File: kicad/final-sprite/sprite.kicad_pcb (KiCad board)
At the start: 4 copper layers, 35 x 44.6 mm, 64 parts, among them J1 M20-7910442R, U1 CC430F513X, U2 LSM9DS1, U3 SPRITETCXO_TCXO_7Z, U4 DRV8837, U5 ADP5092, U6 DRV8837, U7 DRV8837, X1 SPRITEPIN_SPRITE_PIN, X2 SPRITEPIN_SPRITE_PIN

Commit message: Fix inductor
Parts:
- moved TP1 7.53 mm to (136.0, 114.0)
- moved L1 1.99 mm to (126.4, 91.4)
- moved D4 0.63 mm to (143.1, 101.6)
- moved L4 0.17 mm to (141.2, 84.6)
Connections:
- net Net-(L1-PadP$2) renamed /SWN
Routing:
- net Net-(R22-Pad1): track 305.9 -> 310.8 mm, vias 3 -> 4
- net GND: track 14.8 -> 16.0 mm, vias 39 -> 40
- net Net-(L3-Pad1): track 18.5 -> 19.5 mm
- net Net-(L4-Pad2): track 21.6 -> 20.6 mm
- net VCC: track 130.2 -> 129.5 mm
- net /REGGOOD: track 16.8 -> 17.4 mm
- net VCCINT: track 93.9 -> 93.2 mm
- net /RST: track 37.9 -> 38.5 mm
- net (no net): vias 0 -> 1
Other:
- net class Power added: clearance 0.1524, trace_width 0.3048, via_dia 0.5588, via_drill 0.254

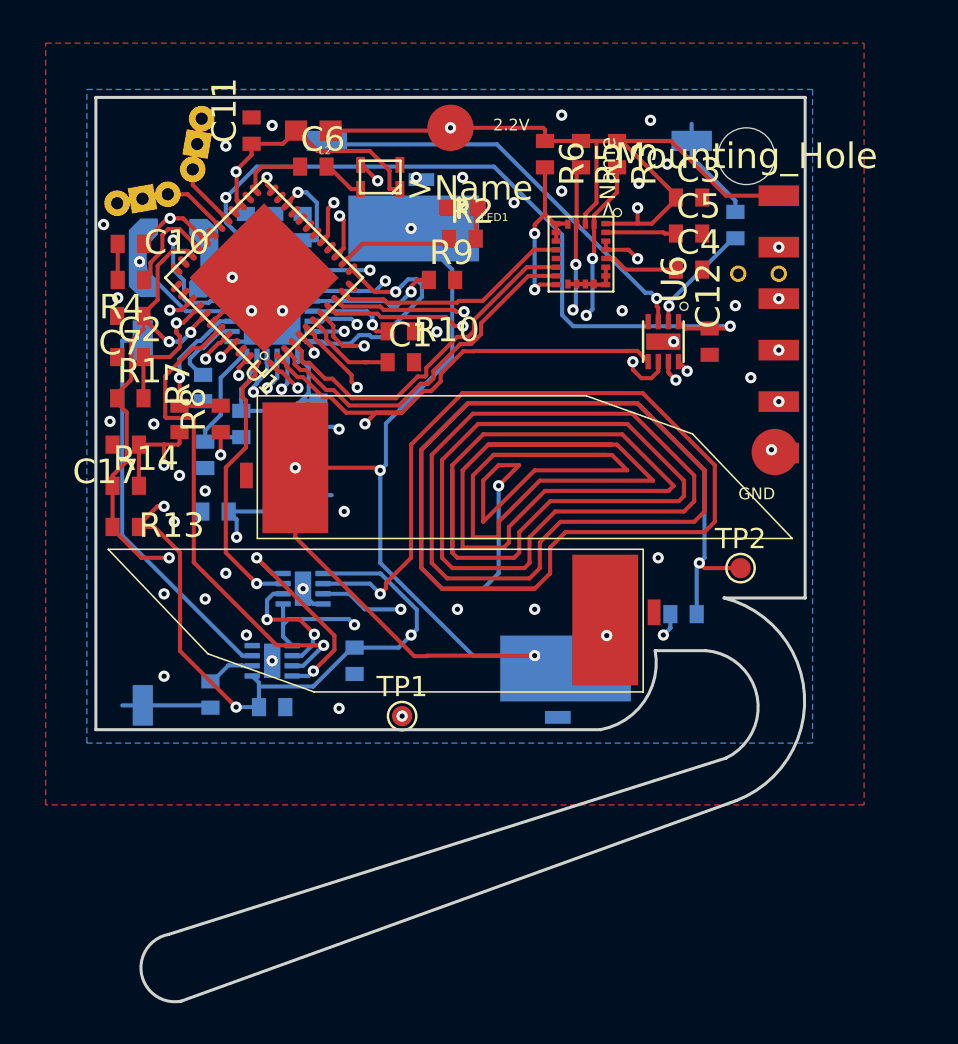
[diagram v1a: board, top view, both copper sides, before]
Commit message: Remove extra test point
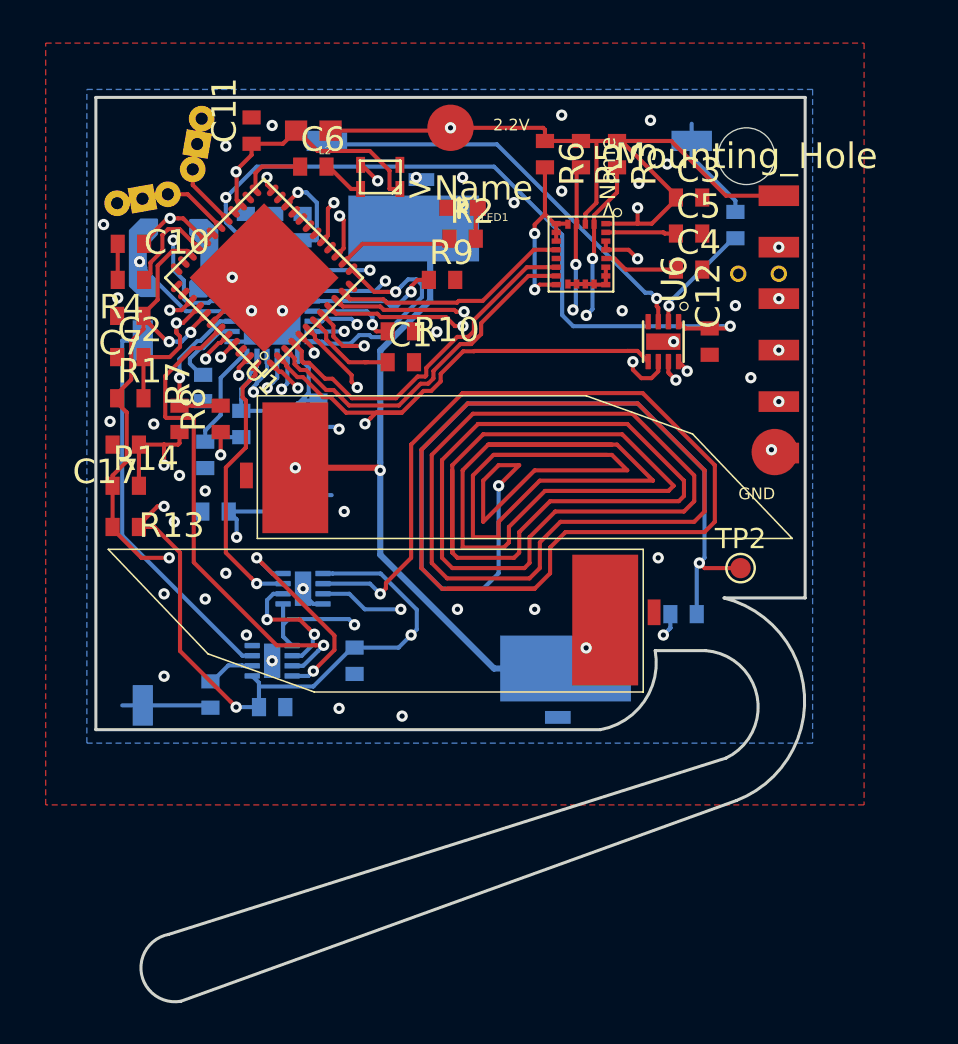
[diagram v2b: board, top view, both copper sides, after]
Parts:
- removed TP1: Test_Point, TestPoint:TestPoint_Pad_D1.0mm
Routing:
- net VCCINT: track 93.2 -> 70.7 mm, vias 7 -> 5
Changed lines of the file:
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@@
     (thickness 0.7874)
     (drawings 24)
-    (tracks 957)
+    (tracks 945)
     (zones 0)
-    (modules 64)
+    (modules 63)
     (nets 70)
   )
@@
     (add_net /UART_RX)
     (add_net /UART_TX)
-    (add_net /VBAT)
     (add_net /VCORE)
     (add_net GND)
@@
     (add_net VCC)
     (add_net VCCA)
-    (add_net VCCINT)
-    (add_net VCCIO)
   )
   (net_class Power ""
@@
     (diff_pair_width 0.1524)
     (add_net /SWN)
-  )
-  (module TestPoint:TestPoint_Pad_D1.0mm (layer Top)
-    (at 135.9535 113.9825)
-    (descr "SMD pad as test Point, diameter 1.0mm")
-    (tags "test point SMD pad")
-    (attr virtual)
-    (fp_text reference TP1 (at 0 -1.448) (layer F.SilkS)
-      (effects (font (size 1 1) (thickness 0.15)))
-    )
-    (fp_text value Test_Point (at 0 1.55) (layer F.Fab)
-      (effects (font (size 1 1) (thickness 0.15)))
-    )
-    (fp_text user %R (at 0 -1.45) (layer F.Fab)
-      (effects (font (size 1 1) (thickness 0.15)))
-    )
-    (fp_circle (center 0 0) (end 1 0) (layer F.CrtYd) (width 0.05))
-    (fp_circle (center 0 0) (end 0 0.7) (layer F.SilkS) (width 0.12))
-    (pad 1 smd circle (at 0 0) (size 1 1) (layers Top F.Mask)
-      (net 66 "Net-(R22-Pad1)"))
+    (add_net /VBAT)
+    (add_net VCCINT)
+    (add_net VCCIO)
   )
   (module sprite:LPS4018-223M (layer Bottom)
@@
   )
   (via (at 121.2215 89.7255) (size 0.5588) (drill 0.254) (layers Top Bottom) (net 0))
+  (via (at 145.034 110.617) (size 0.5588) (drill 0.254) (layers Top Bottom) (net 3))
   (segment (start 143.002 85.048874) (end 143.002 85.602074) (width 0.2032) (layer Top) (net 1) (status 20))
   (segment (start 142.9052 84.952074) (end 143.002 85.048874) (width 0.2032) (layer Top) (net 1))
@@
   (via (at 121.92 93.345) (size 0.5588) (drill 0.254) (layers Top Bottom) (net 2))
   (via (at 127.5715 92.329) (size 0.5588) (drill 0.254) (layers Top Bottom) (net 2))
-  (via (at 136.398 89.916) (size 0.5588) (drill 0.254) (layers Top Bottom) (net 3) (status 30))
-  (via (at 142.494 110.998) (size 0.5588) (drill 0.254) (layers Top Bottom) (net 3) (status 30))
   (via (at 130.683 101.727) (size 0.5588) (drill 0.254) (layers Top Bottom) (net 3) (status 30))
   (segment (start 138.1252 89.919074) (end 136.525 89.919074) (width 0.2032) (layer Bottom) (net 3) (status 30))
@@
   (segment (start 124.968 100.5172) (end 124.968 99.964) (width 0.2032) (layer Top) (net 3) (status 20))
   (segment (start 124.9012 100.584) (end 124.968 100.5172) (width 0.2032) (layer Top) (net 3))
-  (segment (start 130.683 105.156) (end 136.550402 111.023402) (width 0.2032) (layer Top) (net 3))
-  (segment (start 142.098869 110.998) (end 142.494 110.998) (width 0.2032) (layer Top) (net 3))
-  (segment (start 137.162034 111.023402) (end 137.187436 110.998) (width 0.2032) (layer Top) (net 3))
-  (segment (start 130.683 101.727) (end 130.683 105.156) (width 0.2032) (layer Top) (net 3) (status 10))
-  (segment (start 136.550402 111.023402) (end 137.162034 111.023402) (width 0.2032) (layer Top) (net 3))
   (via (at 124.206 101.6) (size 0.5588) (drill 0.254) (layers Top Bottom) (net 3))
   (segment (start 122.966 100.584) (end 124.206 100.584) (width 0.2032) (layer Top) (net 3) (status 10))
@@
   (segment (start 124.206 101.6) (end 124.206 102.364034) (width 0.2032) (layer Route3) (net 3))
   (via (at 134.873998 101.854) (size 0.5588) (drill 0.254) (layers Top Bottom) (net 3))
-  (segment (start 134.746998 101.727) (end 134.873998 101.854) (width 0.2032) (layer Top) (net 3))
-  (segment (start 130.683 101.727) (end 134.746998 101.727) (width 0.2032) (layer Top) (net 3) (status 10))
-  (segment (start 135.153397 99.542603) (end 135.153397 101.574601) (width 0.2032) (layer Bottom) (net 3))
-  (segment (start 135.153397 101.574601) (end 134.873998 101.854) (width 0.2032) (layer Bottom) (net 3))
-  (segment (start 138.424115 96.271885) (end 135.153397 99.542603) (width 0.2032) (layer Bottom) (net 3))
-  (segment (start 138.424115 91.942115) (end 138.424115 96.271885) (width 0.2032) (layer Bottom) (net 3))
-  (segment (start 136.398 89.916) (end 138.424115 91.942115) (width 0.2032) (layer Bottom) (net 3) (status 10))
-  (via (at 146.05 110.00741) (size 0.5588) (drill 0.254) (layers Top Bottom) (net 3) (status 30))
-  (segment (start 143.48459 110.00741) (end 145.654869 110.00741) (width 0.2032) (layer Route3) (net 3))
-  (segment (start 142.494 110.998) (end 143.48459 110.00741) (width 0.2032) (layer Route3) (net 3))
-  (segment (start 134.873998 106.425998) (end 134.873998 102.249131) (width 0.2032) (layer Bottom) (net 3))
-  (segment (start 144.018 110.998) (end 139.446 110.998) (width 0.2032) (layer Bottom) (net 3) (status 10))
-  (segment (start 139.446 110.998) (end 134.873998 106.425998) (width 0.2032) (layer Bottom) (net 3))
   (segment (start 130.683 101.727) (end 130.683 102.588202) (width 0.2032) (layer Bottom) (net 3))
   (segment (start 130.683 102.588202) (end 131.172799 103.078001) (width 0.2032) (layer Bottom) (net 3))
   (segment (start 131.172799 103.078001) (end 132.479201 103.078001) (width 0.2032) (layer Bottom) (net 3))
-  (segment (start 134.873998 102.249131) (end 134.873998 101.854) (width 0.2032) (layer Bottom) (net 3))
-  (segment (start 145.654869 110.00741) (end 146.05 110.00741) (width 0.2032) (layer Route3) (net 3))
-  (segment (start 137.187436 110.998) (end 142.098869 110.998) (width 0.2032) (layer Top) (net 3))
   (segment (start 127.5611 94.002074) (end 125.291873 94.002074) (width 0.2032) (layer Bottom) (net 3))
   (segment (start 123.278899 91.9891) (end 123.278899 91.839211) (width 0.2032) (layer Bottom) (net 3))
@@
   (via (at 122.9995 91.559812) (size 0.5588) (drill 0.254) (layers Top Bottom) (net 3))
   (segment (start 122.9995 100.3935) (end 122.9995 91.954943) (width 0.2032) (layer Route2) (net 3))
+  (segment (start 137.337811 93.471742) (end 134.873998 95.935555) (width 0.3048) (layer Bottom) (net 3))
+  (segment (start 134.873998 101.458869) (end 134.873998 101.854) (width 0.3048) (layer Bottom) (net 3))
+  (segment (start 134.873998 95.935555) (end 134.873998 101.458869) (width 0.3048) (layer Bottom) (net 3))
+  (segment (start 137.337811 90.731885) (end 137.337811 93.471742) (width 0.3048) (layer Bottom) (net 3))
+  (segment (start 136.525 89.919074) (end 137.337811 90.731885) (width 0.3048) (layer Bottom) (net 3))
+  (segment (start 140.4874 111.633) (end 144.018 111.633) (width 0.3048) (layer Bottom) (net 3))
+  (segment (start 134.873998 106.019598) (end 140.4874 111.633) (width 0.3048) (layer Bottom) (net 3))
+  (segment (start 134.873998 101.854) (end 134.873998 106.019598) (width 0.3048) (layer Bottom) (net 3))
+  (segment (start 134.746998 101.727) (end 134.873998 101.854) (width 0.3048) (layer Top) (net 3))
+  (segment (start 130.683 101.727) (end 134.746998 101.727) (width 0.3048) (layer Top) (net 3))
   (segment (start 149.929 94.854) (end 149.594 94.519) (width 0.2032) (layer Top) (net 4) (status 20))
   (segment (start 151.13 94.854) (end 149.929 94.854) (width 0.2032) (layer Top) (net 4) (status 10))

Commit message: Clean up traces
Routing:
- net Net-(R22-Pad1): track 310.8 -> 7.75 mm, vias 4 -> 2
- net Net-(L3-Pad2): track 4.40 -> 0.16 mm
- net VCCINT: track 70.7 -> 67.8 mm
- net Net-(L4-Pad1): track 5.24 -> 4.54 mm
- net (no net): vias 1 -> 0

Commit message: some changes to KiCAD version of things
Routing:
- net VCCINT: track 67.8 -> 84.9 mm, vias 5 -> 6
- net VCC: track 129.5 -> 136.4 mm
- net Net-(R6-Pad2): track 9.61 -> 12.0 mm
- net VCCIO: track 88.5 -> 89.3 mm
- net GND: track 16.0 -> 16.2 mm, vias 40 -> 32

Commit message: Fix footprints and layout
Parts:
- removed C10: 100n, sprite:C0402
- moved C16 5.95 mm to (131.6, 105.7), turned to 0 degrees
- moved C7 3.56 mm to (122.5, 90.7)
- moved R1 1.14 mm to (122.6, 97.2), turned to 180 degrees
- moved C2 1.02 mm to (122.5, 95.2)
- moved D4 0.38 mm to (143.1, 101.2)
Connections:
- net /RST renamed /~RST
- C7 pad 1: VCC -> VCCA
- U1 pad 13: /REG_D1 -> /REG_D0
- U1 pad 15: /REG_D0 -> /REG_D1
- U1 pad 34: VCC -> VCCA
- U5 pad 23: /REG_D0 -> /REG_D1
- U5 pad 24: /REG_D1 -> /REG_D0
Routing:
- net VCCINT: track 84.9 -> 90.4 mm, vias 6 -> 7
- net Net-(L3-Pad2): track 0.16 -> 3.38 mm
- net Net-(R22-Pad1): track 7.75 -> 4.72 mm, vias 2 -> 1
- net VCCIO: track 89.3 -> 87.1 mm
- net /REG_D0: track 9.50 -> 11.5 mm, vias 2 -> 1
- net /SETSD: track 15.6 -> 13.7 mm
- net VCC: track 136.4 -> 137.9 mm, vias 12 -> 4
- net /REG_D1: track 11.4 -> 10.1 mm, vias 1 -> 2
- net /~RST: track 38.9 -> 37.9 mm
- net Net-(R6-Pad2): track 12.0 -> 12.9 mm
- net /PGOOD: track 18.0 -> 18.8 mm
- net GND: track 16.2 -> 15.6 mm, vias 32 -> 28
- net /INT2: track 17.7 -> 17.2 mm
- net VCCA: track 22.0 -> 22.3 mm, vias 2 -> 0

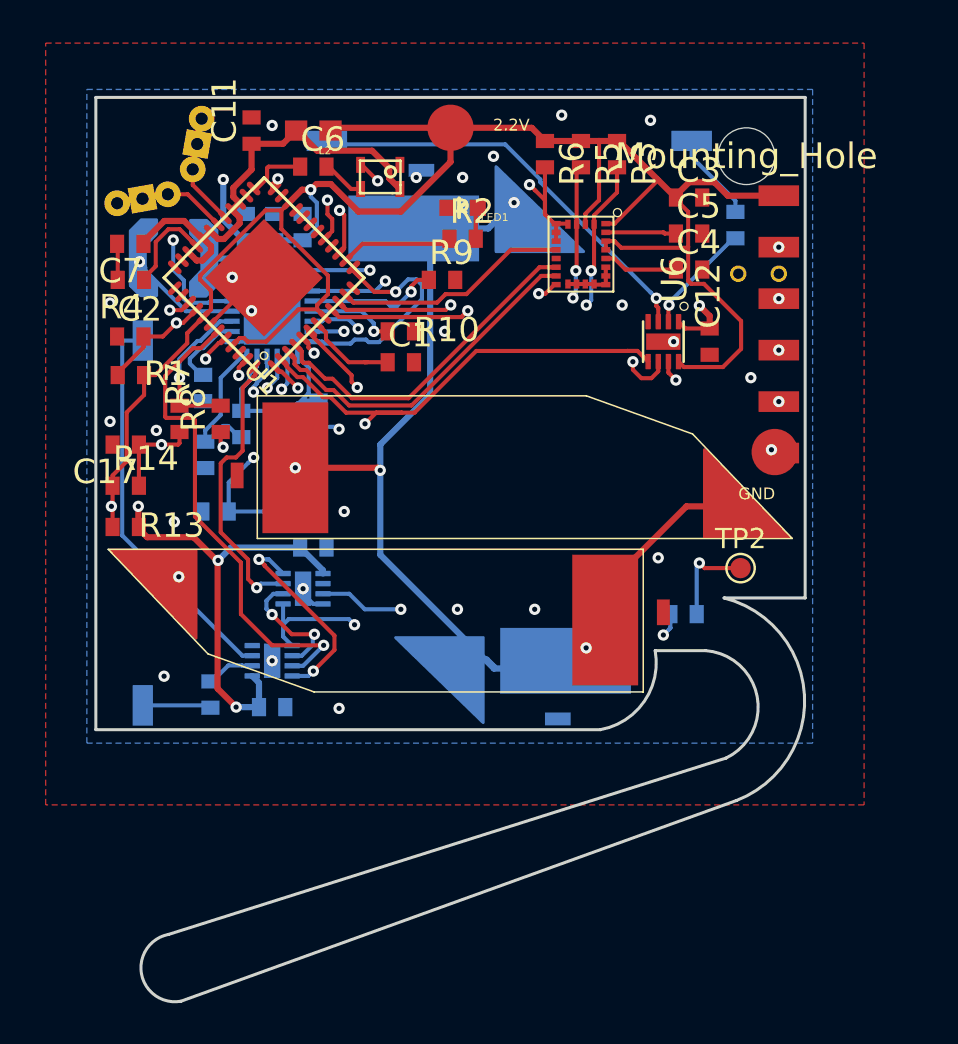
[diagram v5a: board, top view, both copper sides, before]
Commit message: More routing, removed some vias from the bottom layer
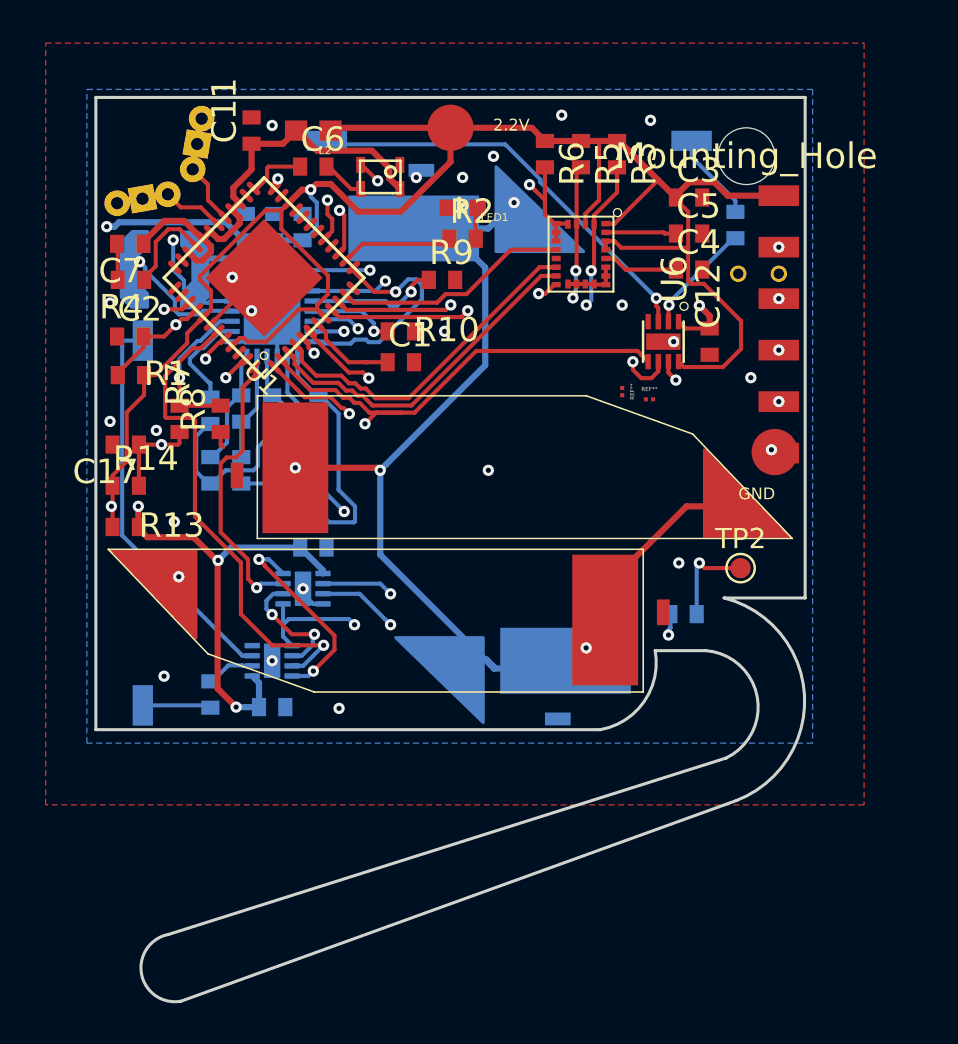
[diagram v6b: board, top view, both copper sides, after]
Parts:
- added REF**: muwave_gap, muwave_gap, F.Cu at (148.2, 98.3)
- added REF**: muwave_gap, muwave_gap, F.Cu at (146.8, 98.0)
- moved R19 5.47 mm to (131.8, 101.9), turned to 90 degrees
- moved R21 4.89 mm to (129.5, 98.8)
- moved R18 4.77 mm to (131.8, 98.8)
- moved R20 3.61 mm to (129.5, 101.9), turned to 270 degrees
- moved R15 2.90 mm to (128.0, 101.9)
- moved C9 1.18 mm to (126.5, 98.9)
- moved R17 0.80 mm to (126.5, 101.9)
- moved R16 0.76 mm to (128.0, 98.8), turned to 270 degrees
- moved L1 0.72 mm to (126.0, 91.9)
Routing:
- net Net-(R22-Pad1): track 4.72 -> 186.2 mm, vias 1 -> 3
- net GND: track 15.6 -> 26.7 mm, vias 28 -> 24
- net VCCIO: track 87.1 -> 79.0 mm
- net /SETSD: track 13.7 -> 5.67 mm, vias 2 -> 0
- net /REF: track 9.28 -> 15.9 mm
- net /TERM: track 10.9 -> 5.72 mm, vias 2 -> 0
- net VCCINT: track 90.4 -> 92.4 mm
- net /SETHYS: track 7.52 -> 5.83 mm
- net Net-(R22-Pad2): track 19.2 -> 20.7 mm
- net Net-(C9-Pad1): track 3.76 -> 5.02 mm
- net /PWM1: track 42.1 -> 41.3 mm
- net /UART_RX: track 25.6 -> 24.8 mm
- net /SETPG: track 4.78 -> 5.35 mm
